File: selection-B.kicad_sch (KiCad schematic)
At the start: 9 parts, among them Q0 Q_NMOS_DGS, Q1 Q_NMOS_DGS, Q2 Q_NMOS_DGS, Q3 Q_NMOS_DGS, U10 74LS08, U15 74LS32, U16 74LS08, U17 74LS08, U18 74HC04

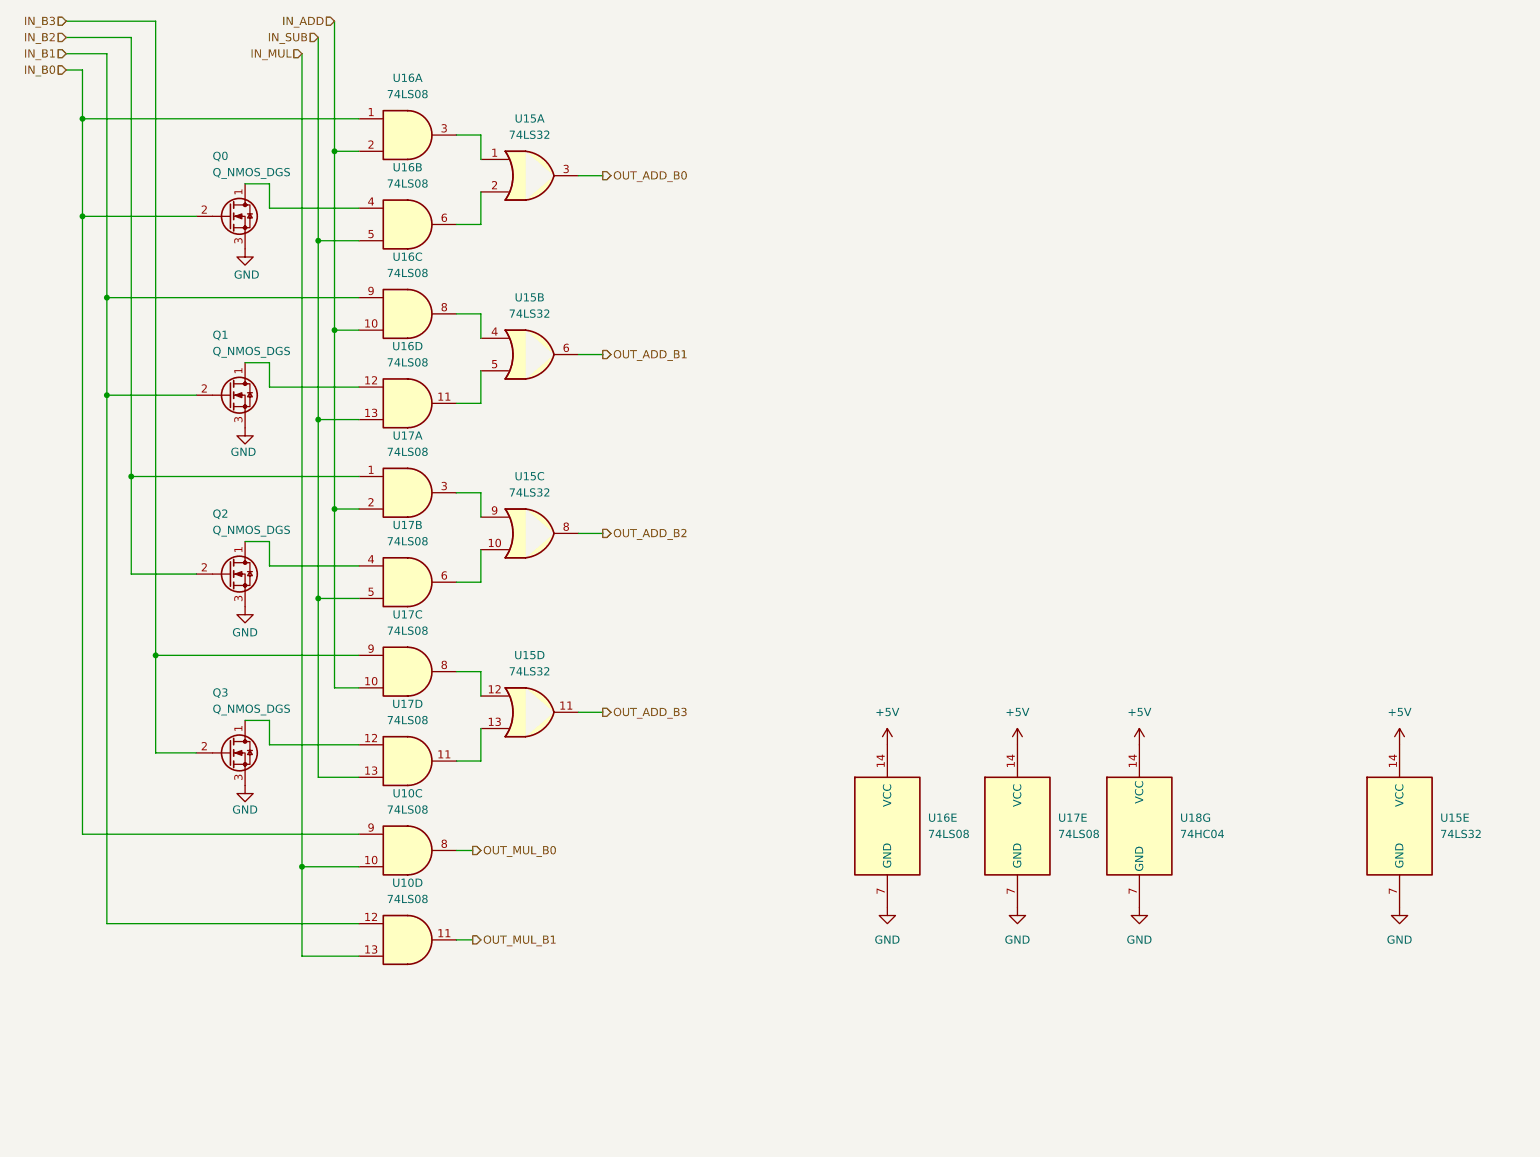
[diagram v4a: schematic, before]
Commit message: feat: footprints on gates
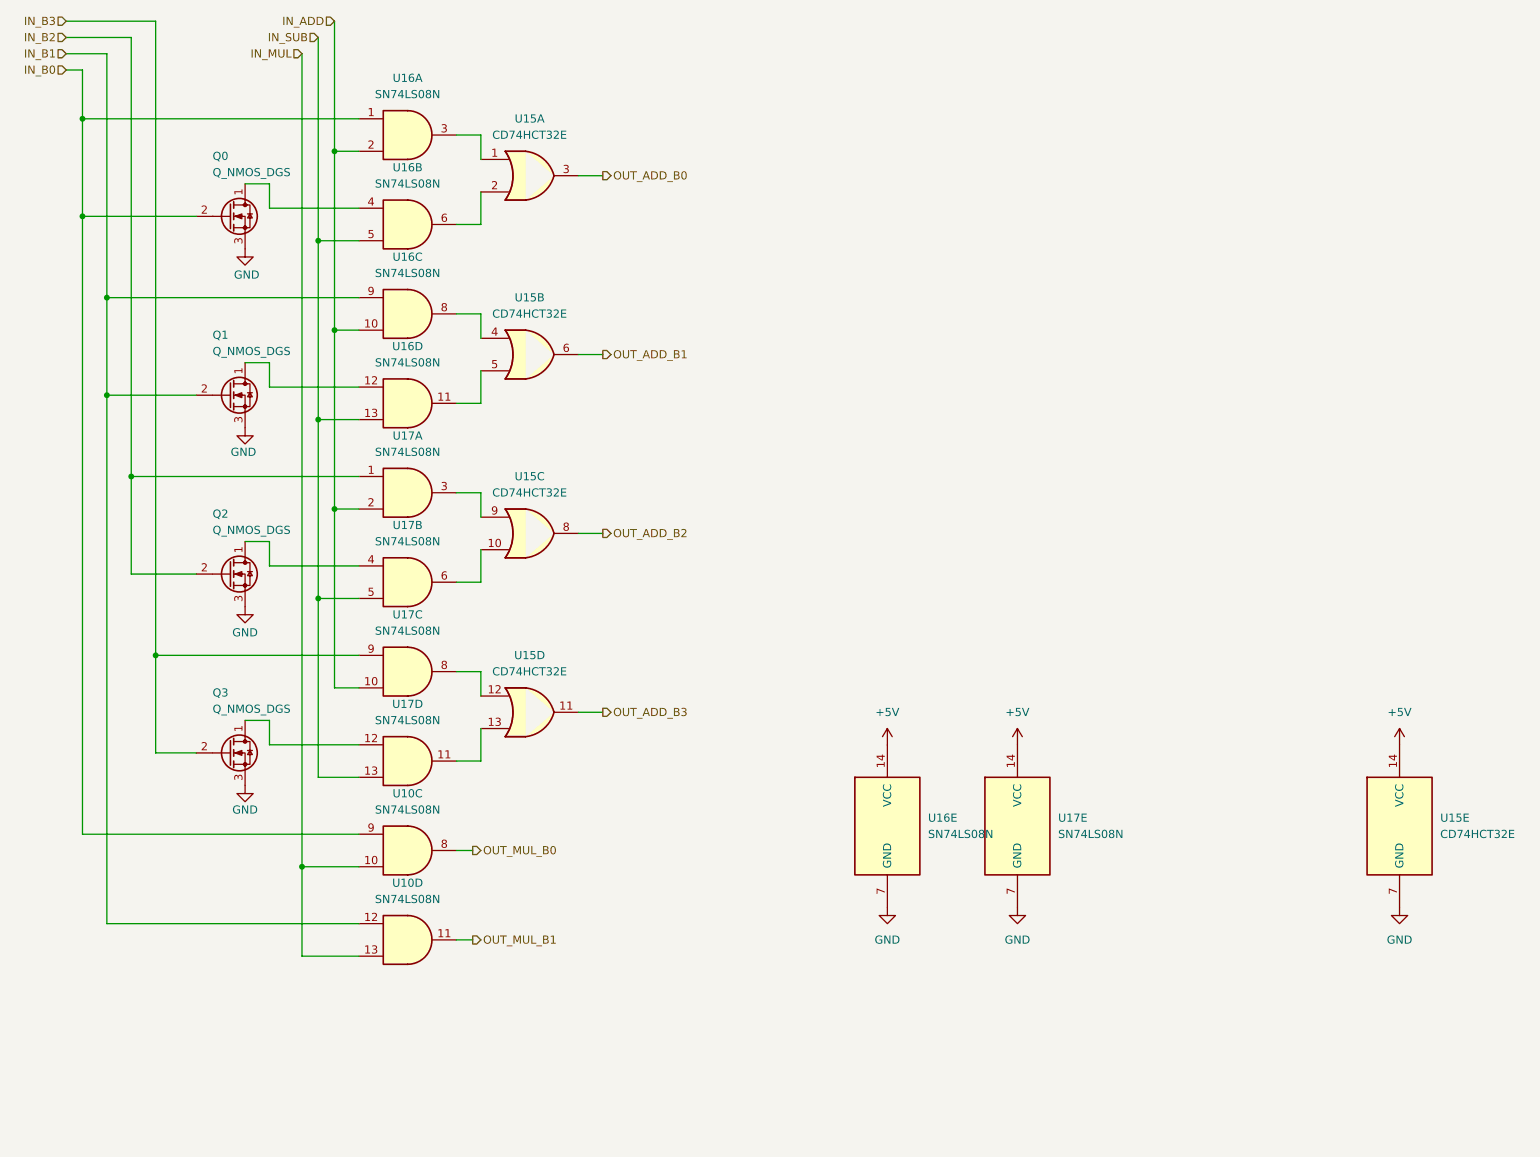
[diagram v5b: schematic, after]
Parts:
- removed U18: 74HC04, symbol 74xx:74HC04
- U10, U16, U17: value 74LS08 -> SN74LS08N; footprint (none) -> Package_DIP:DIP-14_W7.62mm_LongPads
- U15: value 74LS32 -> CD74HCT32E; footprint (none) -> Package_DIP:DIP-14_W7.62mm_LongPads

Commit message: fix: updated footprint for mofset to 23-3 and switch to HandSoldering type
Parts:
- Q0, Q1, Q2, Q3: footprint Package_TO_SOT_SMD:SOT-23 -> Package_TO_SOT_SMD:SOT-23-3
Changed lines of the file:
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@@
 			)
 		)
-		(property "Footprint" "Package_TO_SOT_SMD:SOT-23"
+		(property "Footprint" "Package_TO_SOT_SMD:SOT-23-3"
 			(at 90.17 45.72 0)
 			(hide yes)
@@
 			)
 		)
-		(property "Footprint" "Package_TO_SOT_SMD:SOT-23"
+		(property "Footprint" "Package_TO_SOT_SMD:SOT-23-3"
 			(at 90.17 73.66 0)
 			(hide yes)
@@
 			)
 		)
-		(property "Footprint" "Package_TO_SOT_SMD:SOT-23"
+		(property "Footprint" "Package_TO_SOT_SMD:SOT-23-3"
 			(at 90.17 101.6 0)
 			(hide yes)
@@
 			)
 		)
-		(property "Footprint" "Package_TO_SOT_SMD:SOT-23"
+		(property "Footprint" "Package_TO_SOT_SMD:SOT-23-3"
 			(at 90.17 129.54 0)
 			(hide yes)

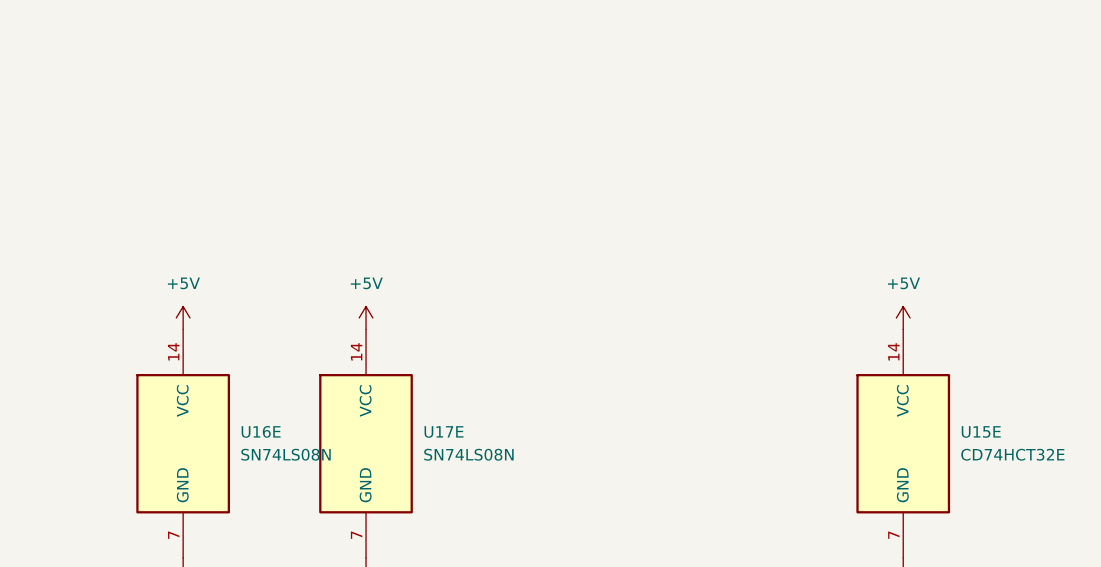
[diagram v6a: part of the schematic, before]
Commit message: feat: added capacitor with footprint
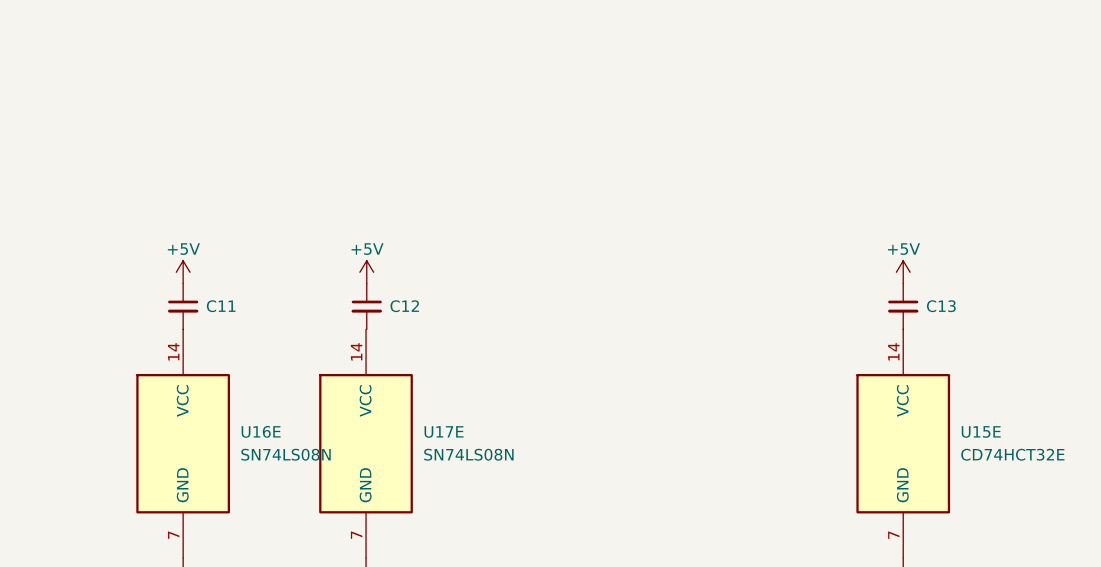
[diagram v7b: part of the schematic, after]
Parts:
- added C11, C12, C13: C_Small, Capacitor_SMD:C_0603_1608Metric_Pad1.08x0.95mm_HandSolder, symbol Device:C_Small
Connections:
- net +5V: now also C11.1, C12.1, C13.1; no longer U15.14 (VCC), U16.14 (VCC), U17.14 (VCC)
- new net: C11.2, U16.14 (VCC)
- new net: C13.2, U15.14 (VCC)

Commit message: fix: merge
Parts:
- renumbered Q0 to Q2, Q1 to Q3, Q2 to Q4, Q3 to Q5, U16 to U11, U17 to U11, U17 to U12, U10 to U12, U15 to U13, U16 to U9
